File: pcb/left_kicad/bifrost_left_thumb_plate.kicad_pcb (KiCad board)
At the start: 2 copper layers, 61.2 x 39.5 mm, 3 parts

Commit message: Update PCB and case designs
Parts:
- PH41: value R0C40 -> 1U
- PH42: value R0C41 -> 1U
- PH43: value R0C42 -> 1U
- moved PH43 22.6 mm to (118.7, 60.6), turned to -6.179 degrees
- moved PH42 15.1 mm to (99.2, 59.5), turned to 0 degrees
- moved PH41 8.12 mm to (79.8, 60.6), turned to 6.179 degrees
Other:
- board size 61.2 x 39.5 mm -> 61.6 x 22.4 mm

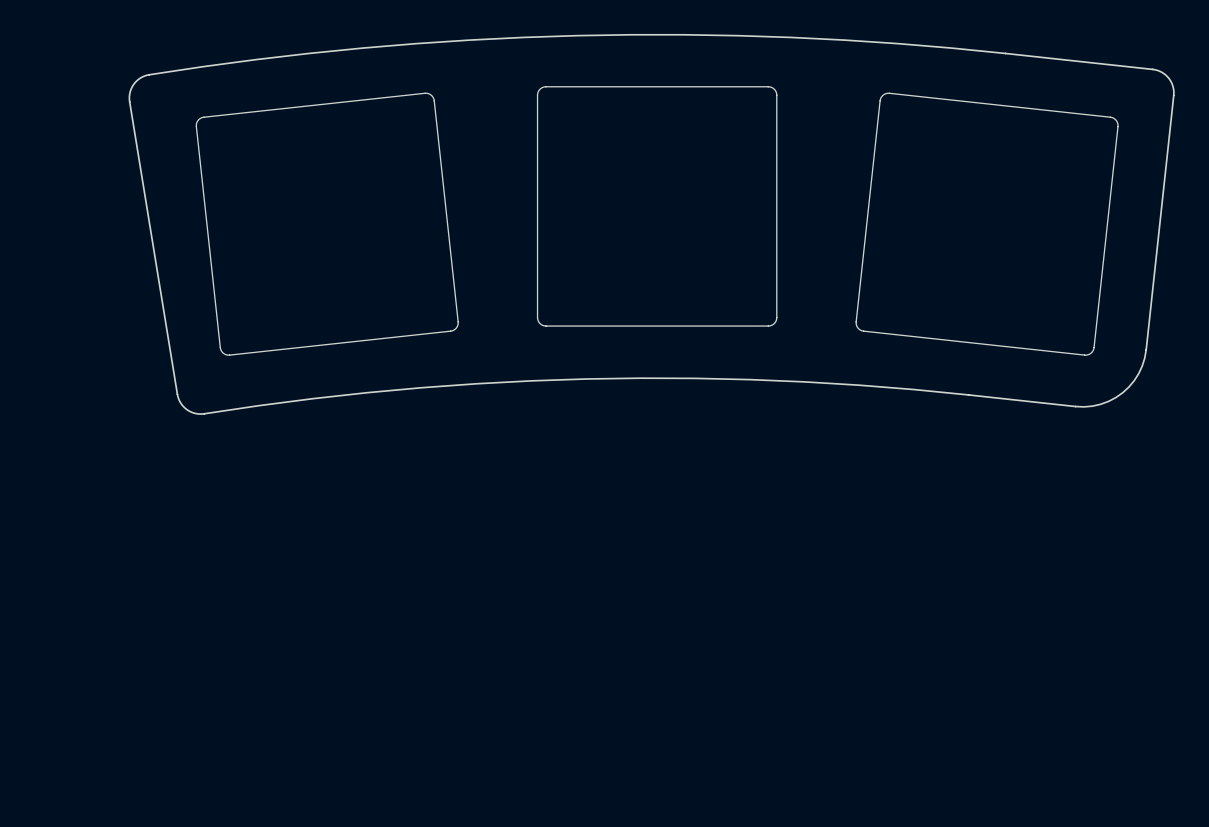
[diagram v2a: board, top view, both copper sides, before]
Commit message: Update case and plate designs
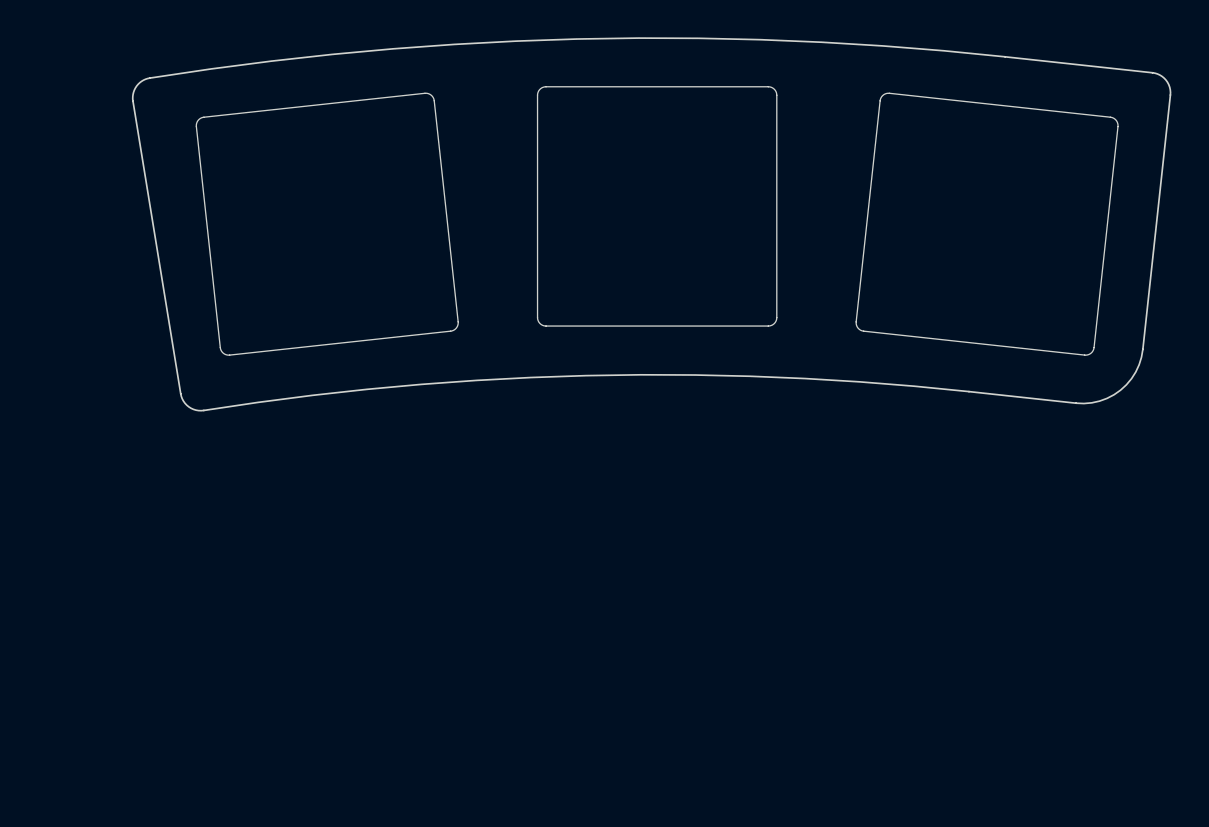
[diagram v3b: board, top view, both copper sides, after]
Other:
- board size 61.6 x 22.4 mm -> 61.2 x 22 mm
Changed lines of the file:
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@@
 	)
 	(gr_arc
-		(start 68.133058 53.369709)
-		(mid 68.378119 52.332446)
-		(end 69.28601 51.774133)
+		(start 68.328902 53.337751)
+		(mid 68.538938 52.448658)
+		(end 69.317151 51.970113)
 		(stroke
 			(width 0.1)
@@
 	)
 	(gr_line
-		(start 68.133058 53.369709)
-		(end 70.945607 70.604395)
+		(start 68.328902 53.337751)
+		(end 71.141453 70.572432)
 		(stroke
 			(width 0.1)
@@
 	)
 	(gr_arc
-		(start 69.28601 51.774133)
-		(mid 94.476176 49.469903)
-		(end 119.749742 50.519069)
+		(start 69.317151 51.970113)
+		(mid 94.48111 49.668283)
+		(end 119.728384 50.716353)
 		(stroke
 			(width 0.1)
@@
 	)
 	(gr_arc
-		(start 72.533925 71.752618)
-		(mid 71.502774 71.506349)
-		(end 70.945607 70.604395)
+		(start 72.50287 71.556624)
+		(mid 71.619008 71.345553)
+		(end 71.141453 70.572432)
 		(stroke
 			(width 0.1)
@@
 	)
 	(gr_arc
-		(start 72.533925 71.752618)
-		(mid 95.015793 69.703374)
-		(end 117.571336 70.642128)
+		(start 72.50287 71.556624)
+		(mid 95.010902 69.50499)
+		(end 117.592695 70.444841)
 		(stroke
 			(width 0.1)
@@
 	)
 	(gr_line
-		(start 117.571336 70.642128)
-		(end 123.884447 71.325605)
+		(start 117.592695 70.444841)
+		(end 123.905805 71.128322)
 		(stroke
 			(width 0.1)
@@
 	)
 	(gr_arc
-		(start 128.038671 67.983014)
-		(mid 126.653824 70.514665)
-		(end 123.884447 71.325605)
+		(start 127.841386 67.961655)
+		(mid 126.529433 70.360073)
+		(end 123.905805 71.128322)
 		(stroke
 			(width 0.1)
@@
 	)
 	(gr_line
-		(start 128.038671 67.983014)
-		(end 129.661935 52.989378)
+		(start 127.841386 67.961655)
+		(end 129.464651 52.968019)
 		(stroke
 			(width 0.1)
@@
 	)
 	(gr_line
-		(start 128.430454 51.458874)
-		(end 119.749742 50.519069)
+		(start 128.409093 51.656159)
+		(end 119.728384 50.716353)
 		(stroke
 			(width 0.1)
@@
 	)
 	(gr_arc
-		(start 128.430454 51.458874)
-		(mid 129.36316 51.969087)
-		(end 129.661935 52.989378)
+		(start 128.409093 51.656159)
+		(mid 129.208565 52.093476)
+		(end 129.464651 52.968019)
 		(stroke
 			(width 0.1)
@@
 	)
 	(group ""
-		(members "348260ae-0aa2-4ecd-a86c-da54100e26ae" "a8c14dc4-6354-48f4-b6bb-95979ecceb49"
-			"b8914473-202f-40a4-bc5f-916c80fa922a" "b951efcf-99c3-4416-9f73-097dc17a7e37"
-			"c46b7a84-1f8e-4f59-9dbc-954914e6be5b" "c4d76932-d06e-42e3-9ca4-7204453c632b"
-			"e9cdf99e-d2ce-4b86-8473-8c0260b50b0c" "f41a7468-9a28-4e88-89e0-574b3602d80b"
-			"faf76b78-ded2-4925-9149-d030c5c65701" "fd0f685f-cafd-4551-938c-45be9253b43c"
+		(members "03b42b54-d0c8-409b-9d9f-2162462759af" "041ee1e2-0107-4a33-ac43-907dad0b4216"
+			"20b190e4-57c9-4f9f-b829-edcd3706ae86" "36609a1c-6a92-4b41-a21a-34c44843d560"
+			"4617769c-d7ad-43e5-bec0-b08224ec4131" "77b979ff-da90-4bbd-89d9-e7ee0bb9dae9"
+			"9449939a-6f5a-4b33-b2a0-7992ef7ab30a" "9a80475b-eded-47b3-af0d-8e72f162eee4"
+			"bc5ae4c0-171f-4042-849d-5262954ecd77" "fca0e028-4e04-45c9-9b70-d8d8831e292c"
 		)
 	)
